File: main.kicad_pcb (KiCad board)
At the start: 2 copper layers, 221.6 x 89.6 mm, 122 parts, among them SW1 Kailh-Choc, SW10 Kailh-Choc, SW11 Kailh-Choc, SW12 Kailh-Choc, SW13 Kailh-Choc, SW14 Kailh-Choc, SW15 Kailh-Choc, SW16 Kailh-Choc, SW17 Kailh-Choc, SW18 Kailh-Choc, SW19 Kailh-Choc, SW2 Kailh-Choc, SW20 Kailh-Choc, SW21 Kailh-Choc, SW22 Kailh-Choc, SW23 Kailh-Choc, SW24 Kailh-Choc, SW25 Kailh-Choc, SW26 Kailh-Choc, SW27 Kailh-Choc, SW28 Kailh-Choc, SW29 Kailh-Choc, SW3 Kailh-Choc, SW30 Kailh-Choc, SW31 Kailh-Choc, SW32 Kailh-Choc, SW33 Kailh-Choc, SW34 Kailh-Choc, SW4 Kailh-Choc, SW5 Kailh-Choc, SW6 Kailh-Choc, SW7 Kailh-Choc, SW8 Kailh-Choc, SW9 Kailh-Choc, U1 nice_nano, U2 nice_nano

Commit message: Various improvements
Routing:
- net R_ROW1: track 133.3 -> 122.5 mm, vias 3 -> 0
- net R_ROW0: track 147.6 -> 139.0 mm, vias 2 -> 0
- net R_COL4: track 134.2 -> 127.2 mm
- net R_ROW2: track 123.4 -> 120.2 mm, vias 1 -> 0

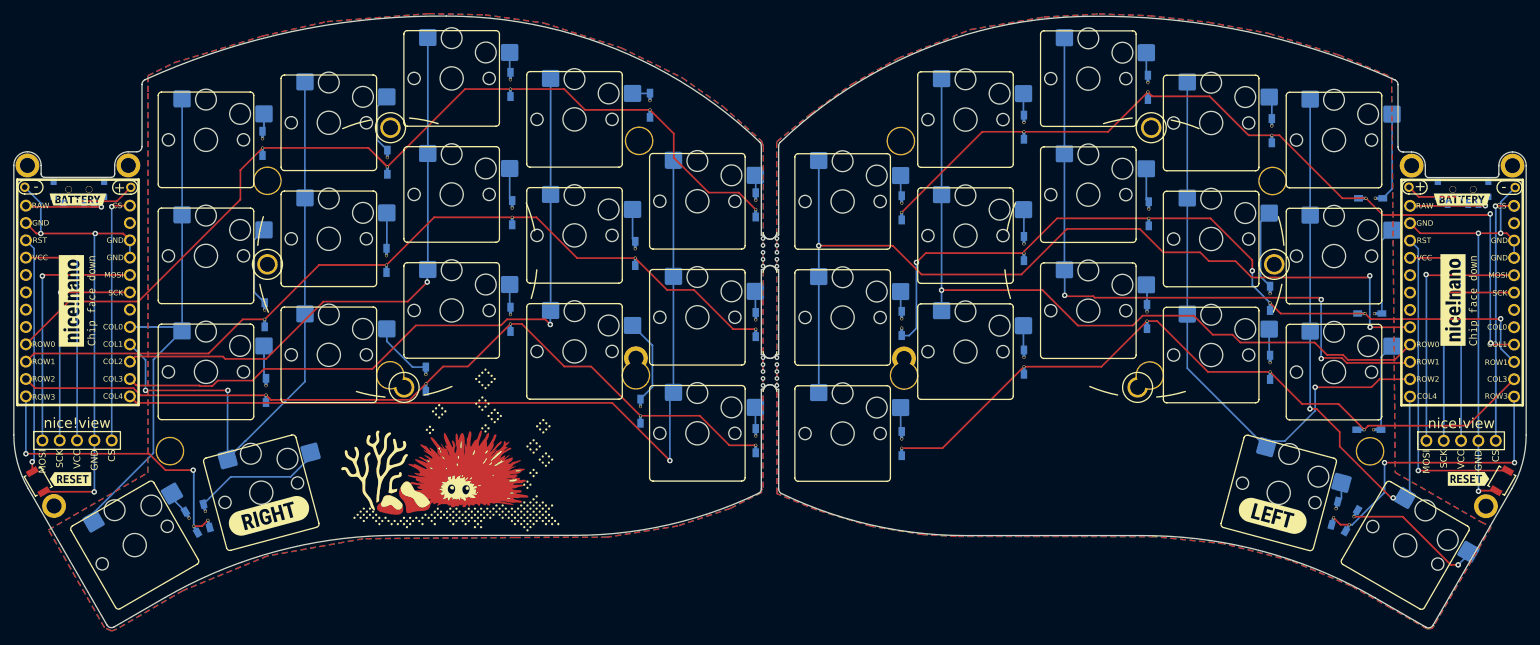
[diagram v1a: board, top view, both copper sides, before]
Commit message: Remode Diode 2nd via & SW17 track on back & Move track from logo
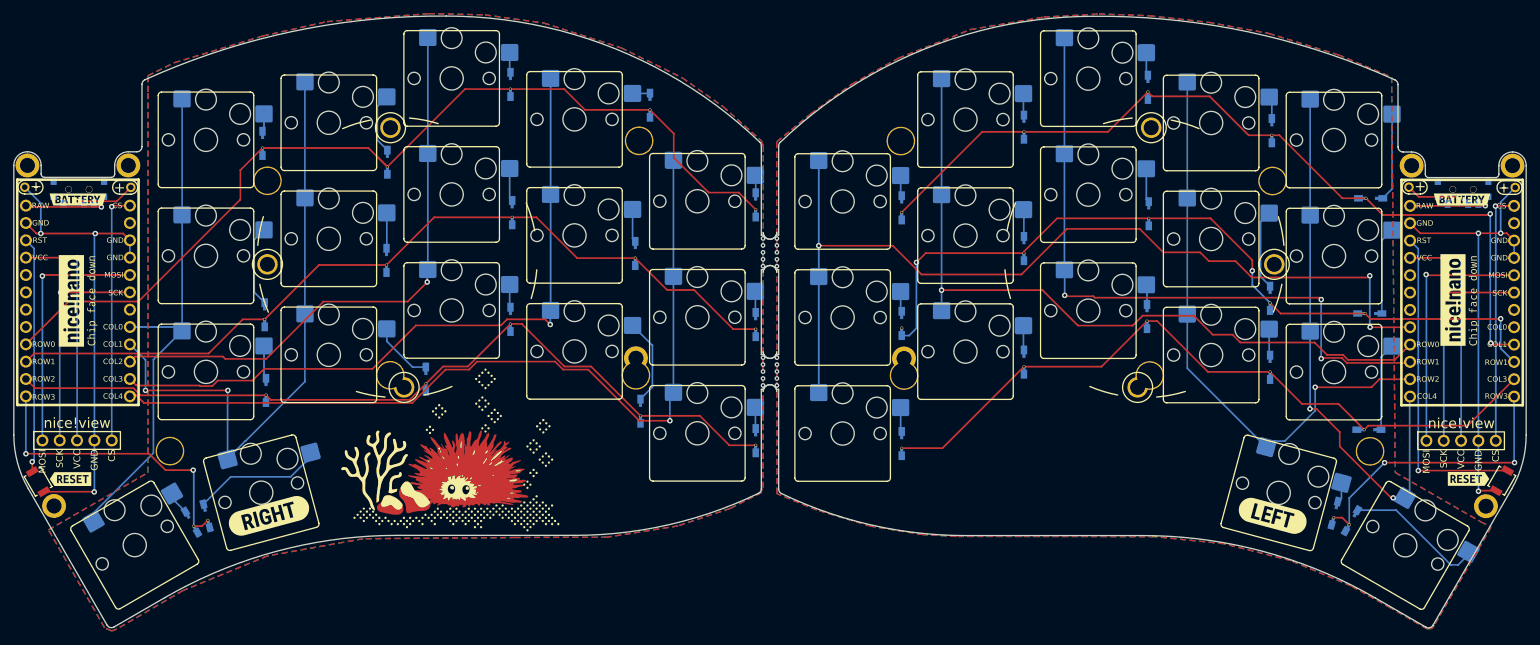
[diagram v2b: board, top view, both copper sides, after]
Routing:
- net R_COL4: track 127.2 -> 124.5 mm
- net Net-(D17-Pad2): track 20.7 -> 20.6 mm, vias 1 -> 0

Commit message: Update to Kicad 8, improve routing, fix DRC
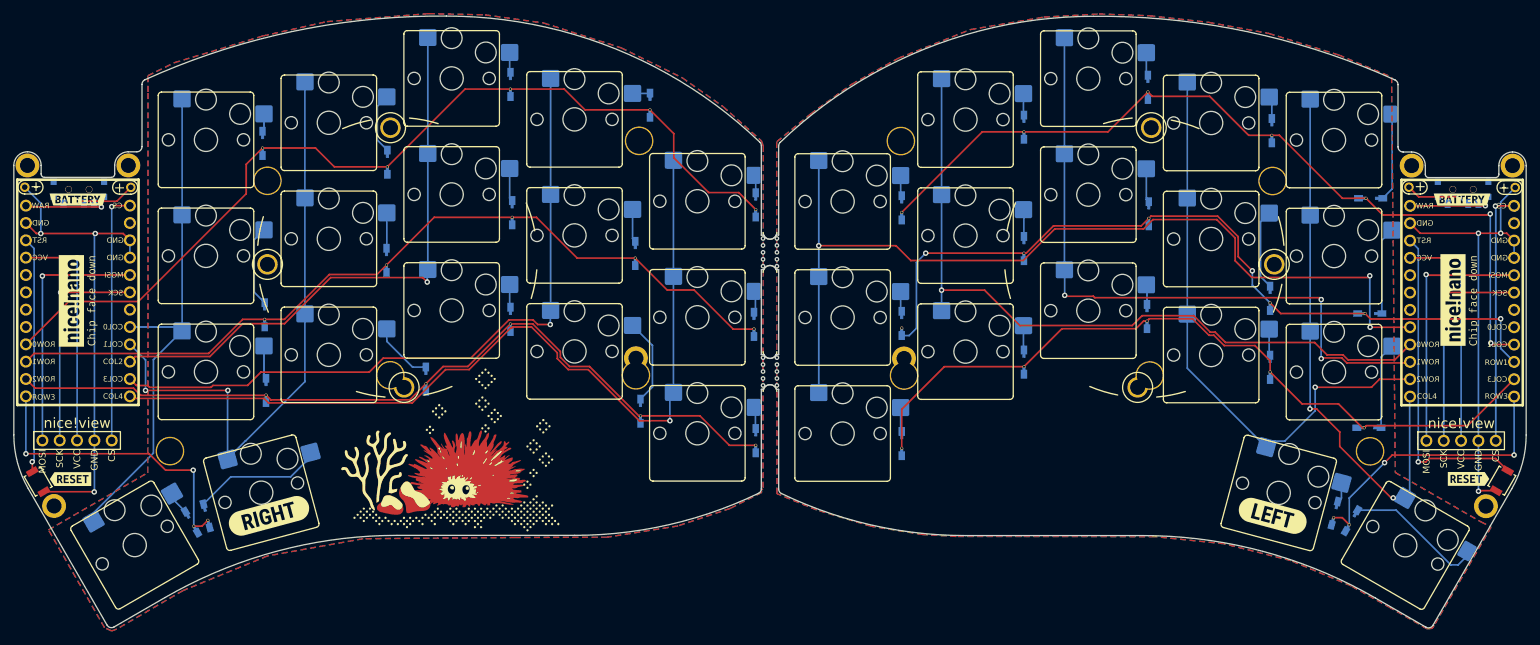
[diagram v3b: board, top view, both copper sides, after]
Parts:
- moved D15 0.29 mm to (216.2, 76.5)
- moved D27 0.26 mm to (126.0, 61.4)
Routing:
- net ROW2: track 107.1 -> 111.4 mm
- net R_COL4: track 124.5 -> 128.7 mm
- net R_ROW0: track 139.0 -> 136.6 mm
- net COL0: track 135.7 -> 137.1 mm
- net ROW1: track 116.1 -> 117.0 mm
- net ROW3: track 42.7 -> 42.0 mm

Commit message: Revert "Update to Kicad 8, improve routing, fix DRC"
This reverts commit f1fb744aeca04b057ba63b33434fe6fbb2a0fd1e.
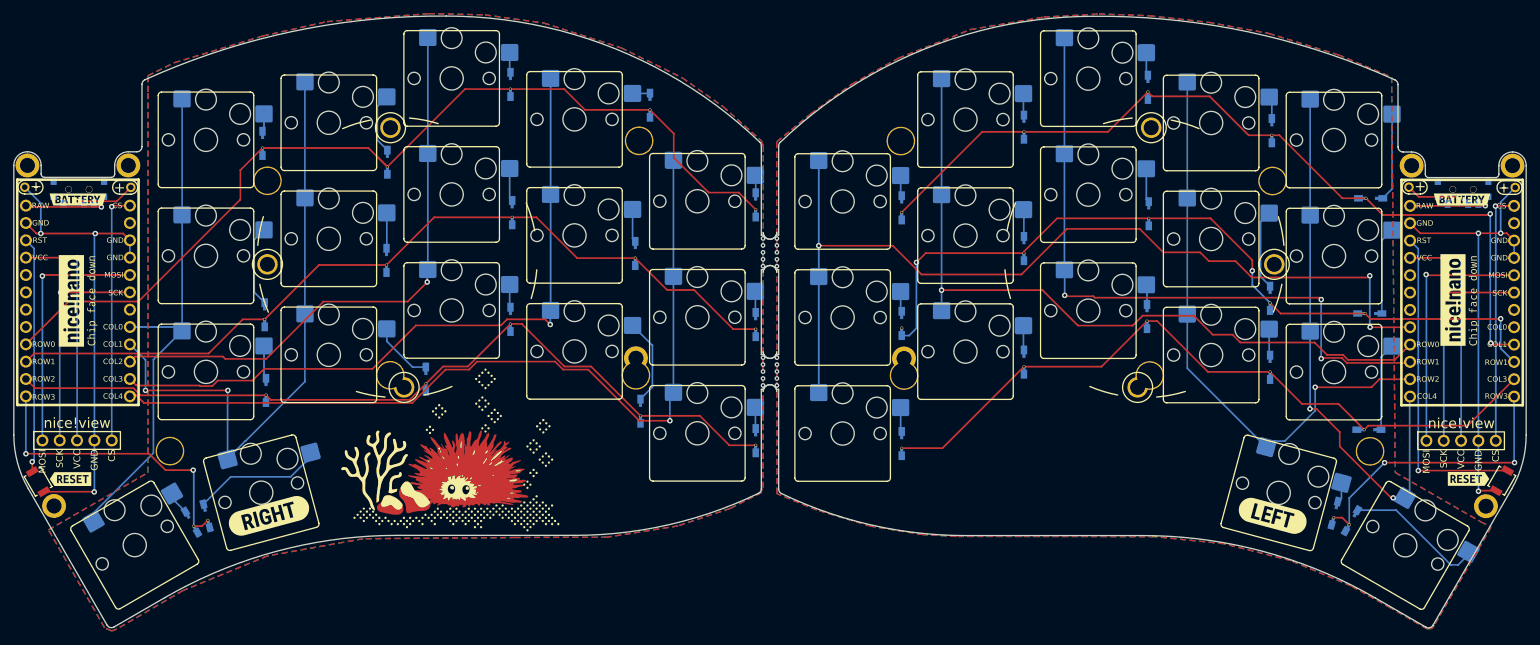
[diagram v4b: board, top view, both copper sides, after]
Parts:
- moved D15 0.29 mm to (216.2, 76.8)
- moved D27 0.26 mm to (126.3, 61.4)
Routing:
- net ROW2: track 111.4 -> 107.1 mm
- net R_COL4: track 128.7 -> 124.5 mm
- net R_ROW0: track 136.6 -> 139.0 mm
- net COL0: track 137.1 -> 135.7 mm
- net ROW1: track 117.0 -> 116.1 mm
- net ROW3: track 42.0 -> 42.7 mm
